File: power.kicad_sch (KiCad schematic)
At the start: 20 parts

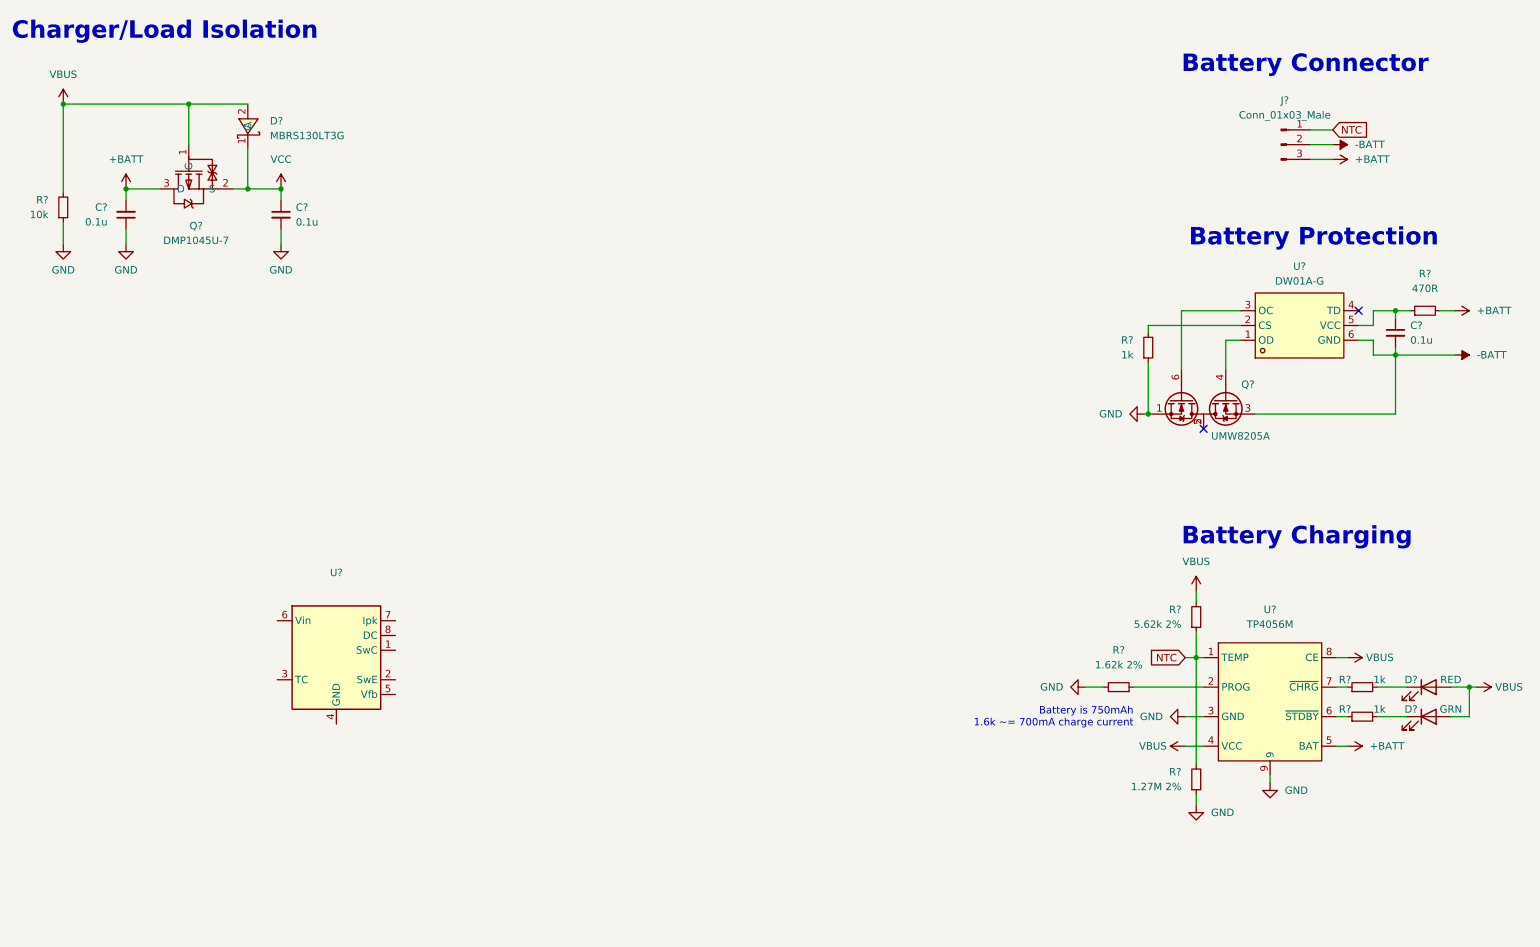
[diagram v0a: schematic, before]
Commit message: schem: finish power design, start SMC design
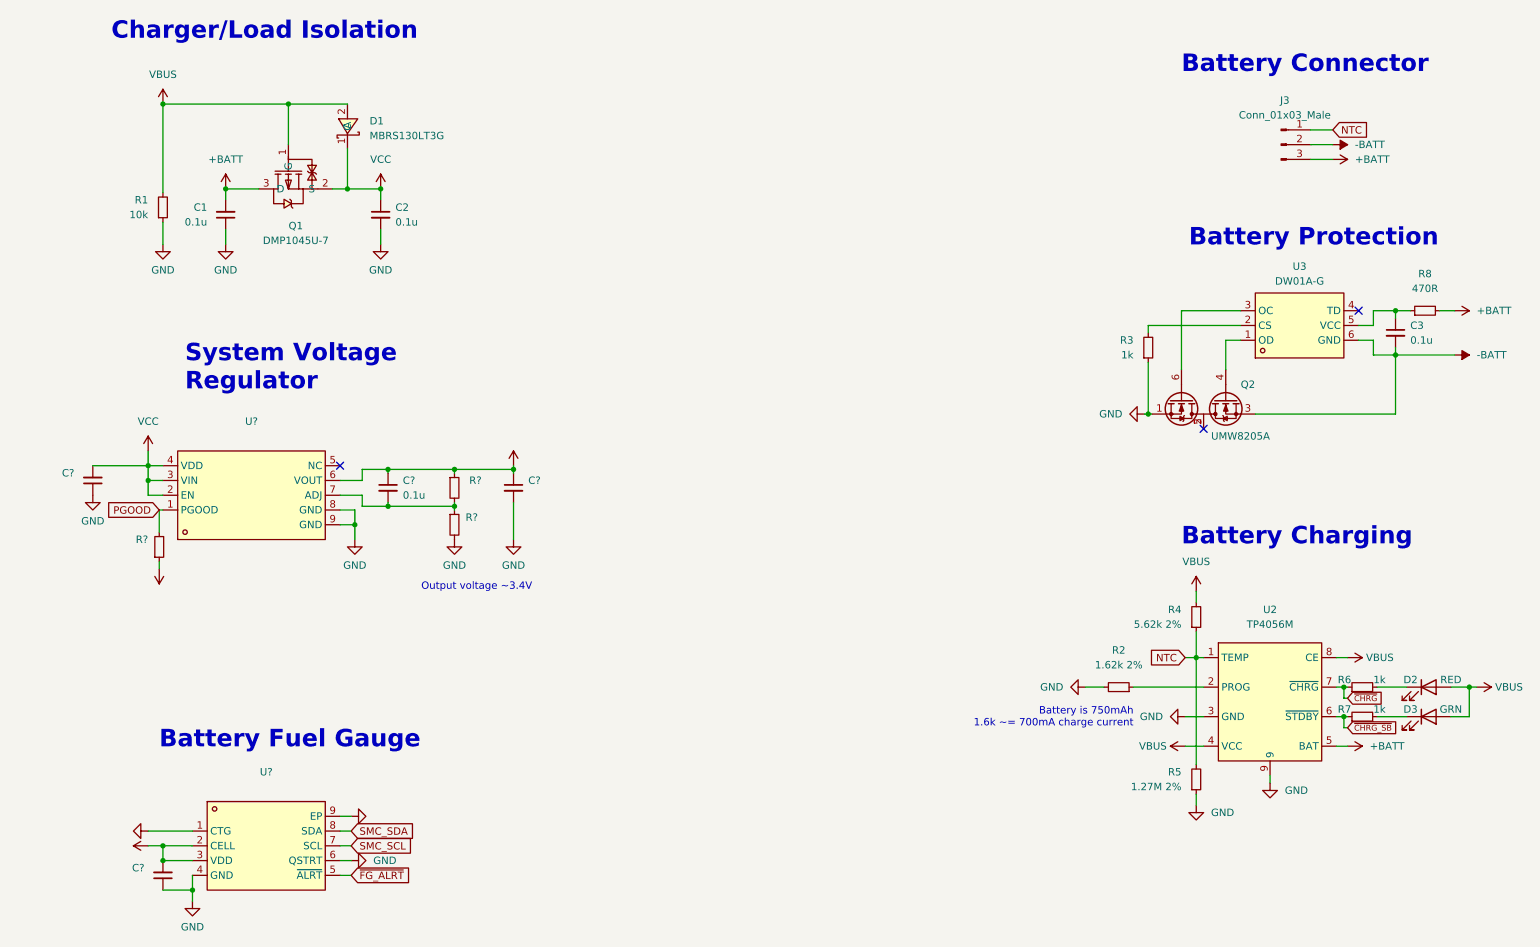
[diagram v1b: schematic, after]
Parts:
- removed U?: (no value), symbol Regulator_Switching:MC34063AD
- added C? (x3): (no value), symbol Device:C_Small
- added C?: 0.1u, symbol Device:C_Small
- added R? (x3): (no value), symbol Device:R_Small
- added U?: (no value), symbol lcsc:TD5830B
- added U?: (no value), lcsc:DFN-8_L2.0-W2.0-P0.50-BL-EP, symbol lcsc:MAX17048G+T10
- gave numbers to parts that had none: 19
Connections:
- net +BATT: now also C?.2, U?.2 (CELL), U?.3 (VDD)
- net GND: now also C?.1, C?.1, C?.2, R?.2, U?.1 (CTG), U?.4 (GND), U?.6 (QSTRT), U?.8 (GND), U?.9 (EP), U?.9 (GND)
- net VCC: now also C?.2, U?.2 (EN), U?.3 (VIN), U?.4 (VDD)
- net ~{CHRG}: now reaches R6.1, U2.7 (~{CHRG})
- net ~{CHRG_SB}: now reaches R7.1, U2.6 (~{STDBY})
- new net: C?.2, R?.1, R?.2, U?.7 (ADJ)
- new net +3V3: C?.1, C?.1, R?.1, R?.1, U?.6 (VOUT)
- new net PGOOD: R?.2, U?.1 (PGOOD)
- new net SMC_SCL: U?.7 (SCL)
- new net SMC_SDA: U?.8 (SDA)
- new net ~{FG_ALRT}: U?.5 (~{ALRT})
- no-connect marks 2 -> 3
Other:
- note added: "Battery Fuel Gauge"
- note added: "Output voltage ~3.4V"
- note added: "System Voltage Regulator"
- moved on the sheet: C1, C2, D1, Q1, R1

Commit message: schem: digital design first pass
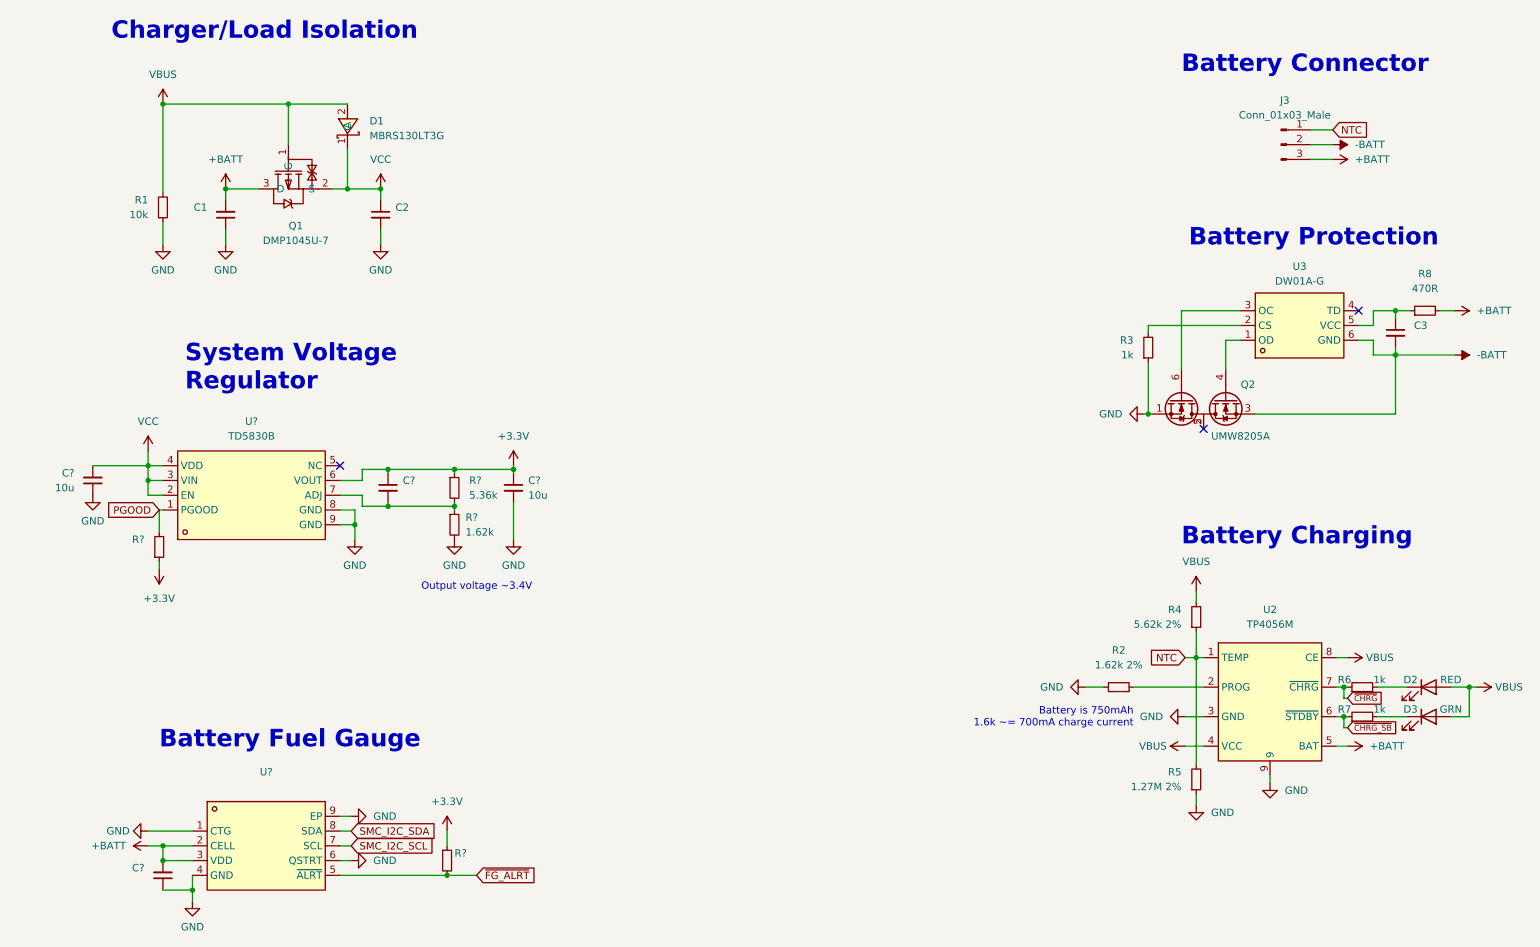
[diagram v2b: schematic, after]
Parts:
- added R?: (no value), symbol Device:R_Small
- C1, C2, C3, C?: value 0.1u -> (none)
- C? (x2): value (none) -> 10u
- R?: value (none) -> 5.36k
- R?: value (none) -> 1.62k
- U?: value (none) -> TD5830B; footprint (none) -> lcsc:SOP-8_L4.9-W3.9-P1.27-LS6.0-BL-EP
- U?: footprint lcsc:DFN-8_L2.0-W2.0-P0.50-BL-EP -> (none)
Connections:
- net +3V3: now also R?.1
- net ~{FG_ALRT}: now also R?.2
- net SMC_SCL renamed SMC_I2C_SCL
- net SMC_SDA renamed SMC_I2C_SDA
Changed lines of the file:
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@@
   (junction (at 95.25 101.6) (diameter 0) (color 0 0 0 0)
+  )
+  (junction (at 93.98 165.1) (diameter 0) (color 0 0 0 0)
   )
   (junction (at 214.63 85.725) (diameter 0) (color 0 0 0 0)
@@
     (stroke (width 0) (type default) (color 0 0 0 0))
   )
+  (wire (pts (xy 93.98 165.1) (xy 99.06 165.1))
+    (stroke (width 0) (type default) (color 0 0 0 0))
+  )
   (wire (pts (xy 247.015 132.715) (xy 248.285 132.715))
     (stroke (width 0) (type default) (color 0 0 0 0))
@@
     (stroke (width 0) (type default) (color 0 0 0 0))
   )
+  (wire (pts (xy 93.98 157.48) (xy 93.98 160.02))
+    (stroke (width 0) (type default) (color 0 0 0 0))
+  )
   (wire (pts (xy 55.88 46.99) (xy 61.595 46.99))
     (stroke (width 0) (type default) (color 0 0 0 0))
@@
     (stroke (width 0) (type default) (color 0 0 0 0))
   )
-  (wire (pts (xy 75.565 165.1) (xy 77.47 165.1))
+  (wire (pts (xy 75.565 165.1) (xy 93.98 165.1))
     (stroke (width 0) (type default) (color 0 0 0 0))
   )
@@
     )
   )
-  (global_label "~{FG_ALRT}" (shape input) (at 77.47 165.1 0) (fields_autoplaced)
+  (global_label "~{FG_ALRT}" (shape input) (at 99.06 165.1 0) (fields_autoplaced)
     (effects (font (size 1.27 1.27)) (justify left))
-    (property "Intersheet References" "${INTERSHEET_REFS}" (id 0) (at 87.5636 165.0206 0)
+    (property "Intersheet References" "${INTERSHEET_REFS}" (id 0) (at 109.1536 165.0206 0)
       (effects (font (size 1.27 1.27)) (justify left) hide)
     )
@@
     )
   )
-  (global_label "SMC_SCL" (shape input) (at 77.47 160.02 0) (fields_autoplaced)
+  (global_label "SMC_I2C_SCL" (shape input) (at 77.47 160.02 0) (fields_autoplaced)
     (effects (font (size 1.27 1.27)) (justify left))
-    (property "Intersheet References" "${INTERSHEET_REFS}" (id 0) (at 88.2893 159.9406 0)
+    (property "Intersheet References" "${INTERSHEET_REFS}" (id 0) (at 92.3412 159.9406 0)
       (effects (font (size 1.27 1.27)) (justify left) hide)
     )
   )
-  (global_label "SMC_SDA" (shape input) (at 77.47 157.48 0) (fields_autoplaced)
+  (global_label "SMC_I2C_SDA" (shape input) (at 77.47 157.48 0) (fields_autoplaced)
     (effects (font (size 1.27 1.27)) (justify left))
-    (property "Intersheet References" "${INTERSHEET_REFS}" (id 0) (at 88.3498 157.4006 0)
+    (property "Intersheet References" "${INTERSHEET_REFS}" (id 0) (at 92.4017 157.4006 0)
       (effects (font (size 1.27 1.27)) (justify left) hide)
     )
@@
       (effects (font (size 1.27 1.27)) (justify right))
     )
-    (property "Value" "" (id 1) (at 29.845 98.4185 0)
+    (property "Value" "10u" (id 1) (at 29.845 98.4185 0)
       (effects (font (size 1.27 1.27)) (justify right))
     )
@@
       (effects (font (size 1.27 1.27)) hide)
     )
-    (property "Value" "" (id 1) (at 44.45 117.475 0))
+    (property "Value" "+3.3V" (id 1) (at 44.45 117.475 0))
     (property "Footprint" "" (id 2) (at 44.45 112.395 0)
       (effects (font (size 1.27 1.27)) hide)
@@
       (effects (font (size 1.27 1.27)) (justify left))
     )
-    (property "Value" "" (id 1) (at 107.95 99.7012 0)
+    (property "Value" "10u" (id 1) (at 107.95 99.7012 0)
       (effects (font (size 1.27 1.27)) (justify left))
     )
@@
     (in_bom yes) (on_board yes) (fields_autoplaced)
     (property "Reference" "U?" (id 0) (at 60.325 86.995 0))
-    (property "Value" "" (id 1) (at 60.325 89.535 0))
-    (property "Footprint" "" (id 2) (at 60.325 86.995 0)
+    (property "Value" "TD5830B" (id 1) (at 60.325 89.535 0))
+    (property "Footprint" "lcsc:SOP-8_L4.9-W3.9-P1.27-LS6.0-BL-EP" (id 2) (at 60.325 86.995 0)
       (effects (font (size 1.27 1.27)) hide)
     )
@@
   (symbol (lib_id "Device:C_Small") (at 257.175 71.755 0) (unit 1)
     (in_bom yes) (on_board yes) (fields_autoplaced)
-    (property "Reference" "C3" (id 0) (at 259.715 70.4912 0)
-      (effects (font (size 1.27 1.27)) (justify left))
-    )
-    (property "Value" "0.1u" (id 1) (at 259.715 73.0312 0)
+    (property "Reference" "C3" (id 0) (at 260.35 70.4912 0)
+      (effects (font (size 1.27 1.27)) (justify left))
+    )
+    (property "Value" "" (id 1) (at 260.35 73.0312 0)
       (effects (font (size 1.27 1.27)) (justify left))
     )
@@
       (effects (font (size 1.27 1.27)) hide)
     )
-    (property "Value" "" (id 1) (at 39.37 157.4799 90)
+    (property "Value" "GND" (id 1) (at 39.37 157.4799 90)
       (effects (font (size 1.27 1.27)) (justify right))
     )
@@
     (pin "1")
   )
+  (symbol (lib_id "power:+3.3V") (at 93.98 157.48 0) (unit 1)
+    (in_bom yes) (on_board yes) (fields_autoplaced)
+    (property "Reference" "#PWR?" (id 0) (at 93.98 161.29 0)
+      (effects (font (size 1.27 1.27)) hide)
+    )
+    (property "Value" "+3.3V" (id 1) (at 93.98 152.4 0))
+    (property "Footprint" "" (id 2) (at 93.98 157.48 0)
+      (effects (font (size 1.27 1.27)) hide)
+    )
+    (property "Datasheet" "" (id 3) (at 93.98 157.48 0)
+      (effects (font (size 1.27 1.27)) hide)
+    )
+    (pin "1")
+  )
   (symbol (lib_id "power:GND") (at 203.835 132.715 270) (unit 1)
     (in_bom yes) (on_board yes) (fields_autoplaced)
@@
   (symbol (lib_id "Device:R_Small") (at 44.45 108.585 0) (mirror x) (unit 1)
     (in_bom yes) (on_board yes) (fields_autoplaced)
-    (property "Reference" "R?" (id 0) (at 42.545 107.3149 0)
-      (effects (font (size 1.27 1.27)) (justify right))
-    )
-    (property "Value" "" (id 1) (at 42.545 109.8549 0)
+    (property "Reference" "R?" (id 0) (at 41.91 107.3149 0)
+      (effects (font (size 1.27 1.27)) (justify right))
+    )
+    (property "Value" "" (id 1) (at 41.91 109.8549 0)
       (effects (font (size 1.27 1.27)) (justify right))
     )
@@
       (effects (font (size 1.27 1.27)) (justify right))
     )
-    (property "Value" "0.1u" (id 1) (at 52.705 52.6985 0)
+    (property "Value" "" (id 1) (at 52.705 52.6985 0)
       (effects (font (size 1.27 1.27)) (justify right))
     )
@@
     (pin "2")
   )
+  (symbol (lib_id "Device:R_Small") (at 93.98 162.56 0) (unit 1)
+    (in_bom yes) (on_board yes)
+    (property "Reference" "R?" (id 0) (at 95.25 161.29 0)
+      (effects (font (size 1.27 1.27)) (justify left))
+    )
+    (property "Value" "" (id 1) (at 95.25 163.83 0)
+      (effects (font (size 1.27 1.27)) (justify left))
+    )
+    (property "Footprint" "" (id 2) (at 93.98 162.56 0)
+      (effects (font (size 1.27 1.27)) hide)
+    )
+    (property "Datasheet" "~" (id 3) (at 93.98 162.56 0)
+      (effects (font (size 1.27 1.27)) hide)
+    )
+    (pin "1")
+    (pin "2")
+  )
   (symbol (lib_id "power:GND") (at 77.47 154.94 90) (unit 1)
     (in_bom yes) (on_board yes) (fields_autoplaced)
@@
       (effects (font (size 1.27 1.27)) hide)
     )
-    (property "Value" "" (id 1) (at 81.28 154.9399 90)
+    (property "Value" "GND" (id 1) (at 81.28 154.9399 90)
       (effects (font (size 1.27 1.27)) (justify right))
     )
@@
       (effects (font (size 1.27 1.27)) (justify left))
     )
-    (property "Value" "" (id 1) (at 97.79 99.6949 0)
+    (property "Value" "5.36k" (id 1) (at 97.79 99.6949 0)
       (effects (font (size 1.27 1.27)) (justify left))
     )
@@
       (effects (font (size 1.27 1.27)) hide)
     )
-    (property "Value" "" (id 1) (at 38.735 160.0199 90)
+    (property "Value" "+BATT" (id 1) (at 38.735 160.0199 90)
       (effects (font (size 1.27 1.27)) (justify left))
     )
@@
       (effects (font (size 1.27 1.27)) (justify left))
     )
-    (property "Value" "0.1u" (id 1) (at 86.36 99.7012 0)
+    (property "Value" "" (id 1) (at 86.36 99.7012 0)
       (effects (font (size 1.27 1.27)) (justify left))
     )
@@
       (effects (font (size 1.27 1.27)) hide)
     )
-    (property "Value" "" (id 1) (at 105.41 89.535 0))
+    (property "Value" "+3.3V" (id 1) (at 105.41 89.535 0))
     (property "Footprint" "" (id 2) (at 105.41 94.615 0)
       (effects (font (size 1.27 1.27)) hide)
@@
       (effects (font (size 1.27 1.27)) (justify left))
     )
-    (property "Value" "" (id 1) (at 97.155 106.0449 0)
+    (property "Value" "1.62k" (id 1) (at 97.155 106.0449 0)
       (effects (font (size 1.27 1.27)) (justify left))
     )
@@
       (effects (font (size 1.27 1.27)) (justify left))
     )
-    (property "Value" "0.1u" (id 1) (at 85.09 52.7112 0)
+    (property "Value" "" (id 1) (at 85.09 52.7112 0)
       (effects (font (size 1.27 1.27)) (justify left))
     )
@@
     (property "Reference" "U?" (id 0) (at 62.865 147.32 0))
     (property "Value" "" (id 1) (at 62.865 149.86 0))
-    (property "Footprint" "lcsc:DFN-8_L2.0-W2.0-P0.50-BL-EP" (id 2) (at 62.865 172.72 0)
-      (effects (font (size 1.27 1.27)) hide)
-    )
+    (property "Footprint" "" (id 2) (at 62.865 172.72 0)
+      (effects (font (size 1.27 1.27)) hide)
+    )
